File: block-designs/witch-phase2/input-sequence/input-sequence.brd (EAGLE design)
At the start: 160 x 100 mm, 21 parts, among them IC1 74AHC1G08DBV, IC10 741G175, IC11 741G175, IC12 741G175, IC13 74AHC1G32DBV, IC14 74AHC1G32DBV, IC15 74AHC1G32DBV, IC16 74AHC1G32DBV, IC17 74AHC1G32DBV, IC18 74AHC1G32DBV, IC19 4017D, IC2 74AHC1G08DBV, IC3 74AHC1G08DBV, IC4 74AHC1G08DBV, IC5 74AHC1G08DBV, IC6 74AHC1G08DBV, IC7 741G175, IC8 741G175, IC9 741G175

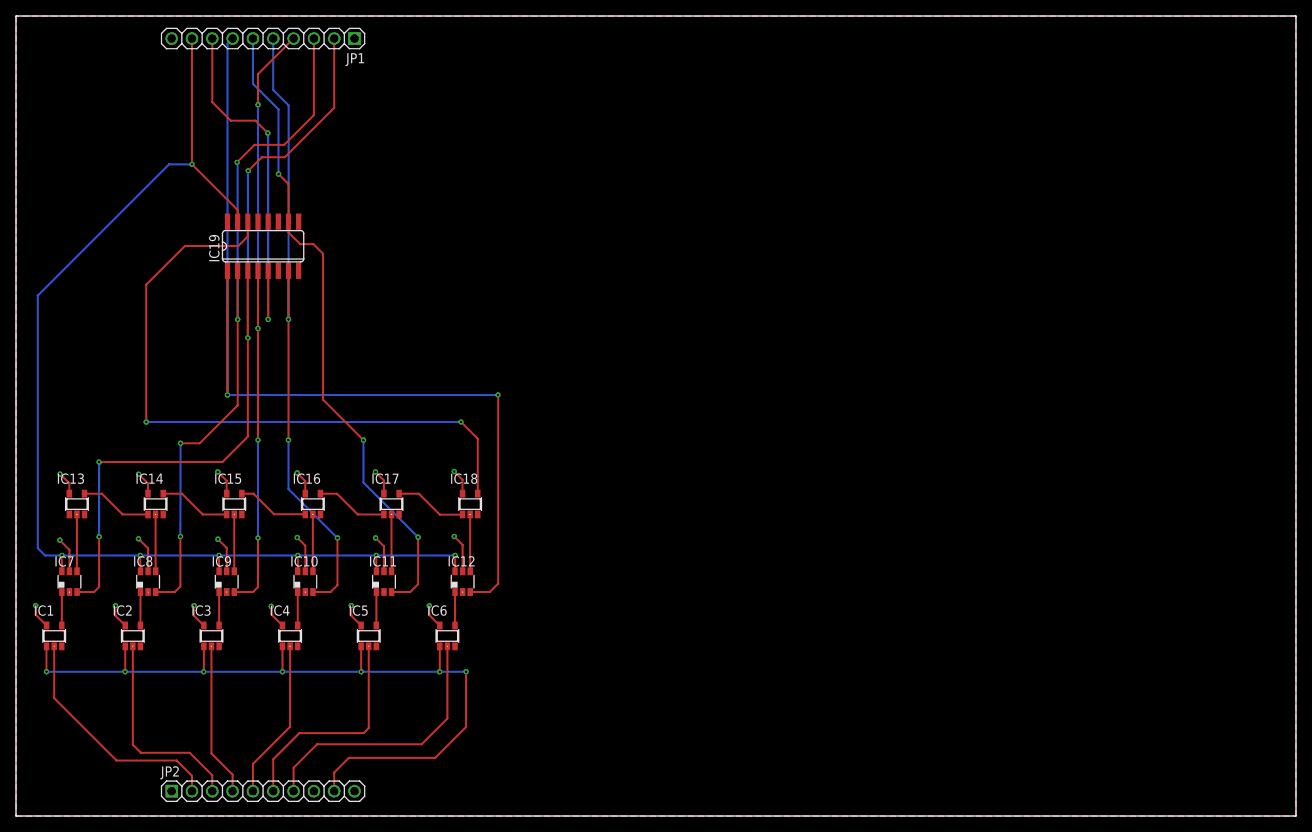
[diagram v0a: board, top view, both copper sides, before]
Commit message: reduce pcb size, add caps, add LEDs
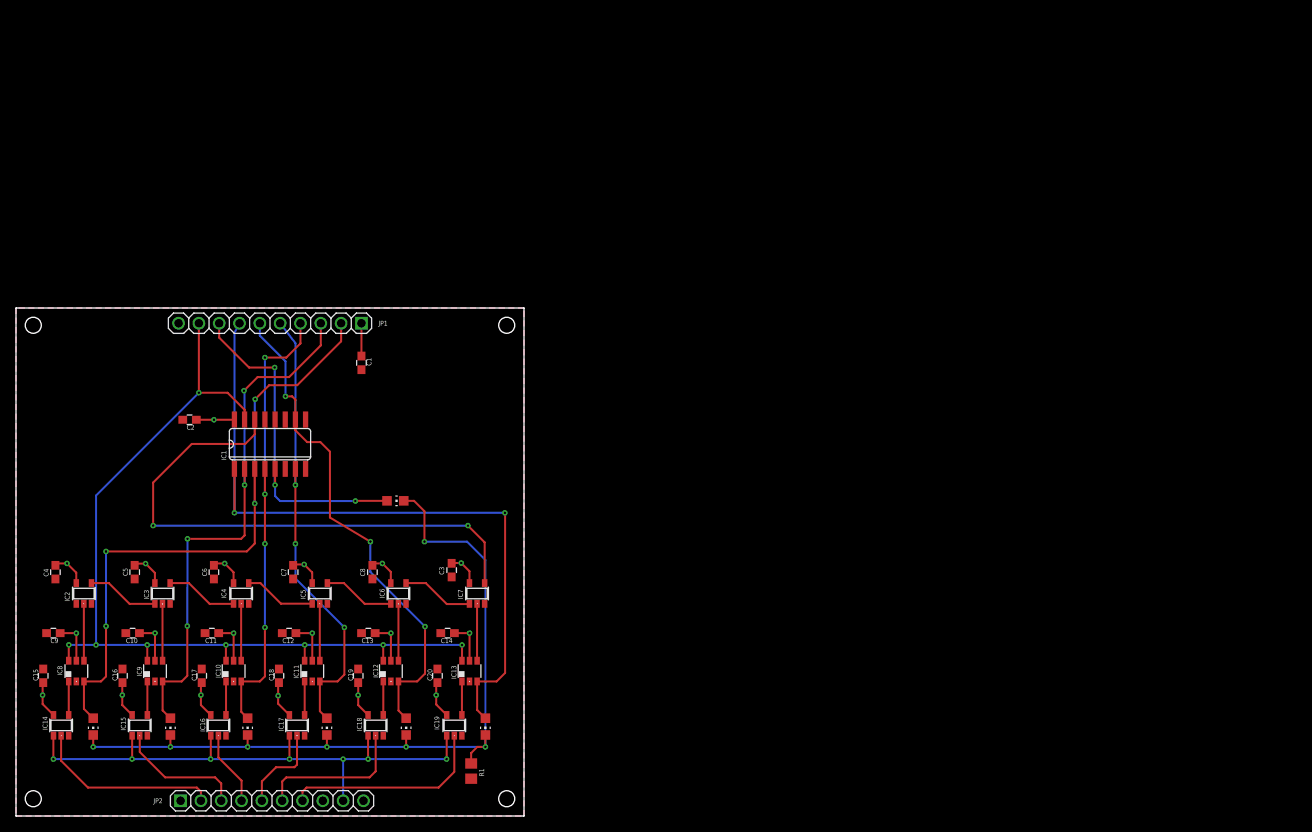
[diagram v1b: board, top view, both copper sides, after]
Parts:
- added C1, C10, C11, C12, C13, C14, C15, C16, C17, C18, C19, C2, C20, C3, C4, C5, C6, C7, C8, C9: 0.1uF, resistor:C0603
- added LED1, LED2, LED3, LED4, LED5, LED6, LED7: RED, led:CHIP-LED0805
- added R1: (no value), resistor:R0805
- IC1: value 74AHC1G08DBV -> 4017D; device 74xx-little-us:SOT23-5 -> 40xx:SO16
- IC13: value 74AHC1G32DBV -> 741G175; device 74xx-little-us:SOT23-5 -> witch-e:DBV_R-PDSO-G6
- IC14, IC15, IC16, IC17, IC18: value 74AHC1G32DBV -> 74AHC1G08DBV
- IC19: value 4017D -> 74AHC1G08DBV; device 40xx:SO16 -> 74xx-little-us:SOT23-5
- IC2, IC3, IC4, IC5, IC6: value 74AHC1G08DBV -> 74AHC1G32DBV
- IC7: value 741G175 -> 74AHC1G32DBV; device witch-e:DBV_R-PDSO-G6 -> 74xx-little-us:SOT23-5
- moved IC19 64.5 mm to (54.8, 11.3)
- moved IC13 53.3 mm to (56.7, 18.1)
- moved IC7 51.0 mm to (57.6, 27.8)
- moved IC1 36.1 mm to (31.8, 46.5)
- moved JP1 35.6 mm to (31.8, 61.6)
- moved IC14 30.1 mm to (5.64, 11.3)
- moved IC15 30.1 mm to (15.5, 11.3)
- moved IC16 30.1 mm to (25.3, 11.3)
- moved IC17 30.1 mm to (35.1, 11.3)
- moved IC18 30.1 mm to (45.0, 11.3)
- moved IC10 14.3 mm to (27.2, 18.1)
- moved IC11 14.3 mm to (37.0, 18.1)
- moved IC12 14.3 mm to (46.9, 18.1)
- moved IC8 14.3 mm to (7.54, 18.1)
- moved IC9 14.3 mm to (17.4, 18.1)
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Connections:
- removed net VDD: IC19.16
- removed net VSS: IC19.8
- new net LED_SINK: LED1.C, LED2.C, LED3.C, LED4.C, LED5.C, LED6.C, LED7.C, R1.2
- net !MCLK: now also IC14.1, IC15.1, IC16.1, IC17.1, IC18.1, IC19.1; no longer IC1.1, IC2.1, IC3.1, IC4.1, IC5.1, IC6.1
- net !RESET: now also IC1.15, IC13.6; no longer IC19.15, IC7.6
- net GND: now also C1.2, C10.2, C11.2, C12.2, C13.2, C14.2, C15.2, C16.2, C17.2, C18.2, C19.2, C2.2, C20.2, C3.2, C4.2, C5.2, C6.2, C7.2, C8.2, C9.2, IC1.13, IC1.8, IC13.2, IC19.3, IC2.1, IC7.3, R1.1; no longer IC1.3, IC13.1, IC13.3, IC19.13, IC7.2
- net N$1: now also IC15.4, IC9.1; no longer IC2.4, IC8.1
- net N$2: now also IC14.4, IC8.1; no longer IC1.4, IC7.1
- net N$3: now also IC10.1, IC16.4; no longer IC3.4, IC9.1
- net N$4: now also IC11.1, IC17.4; no longer IC10.1, IC4.4
- net N$5: now also IC12.1, IC18.4; no longer IC11.1, IC5.4
- net N$6: now also IC13.1, IC19.4; no longer IC12.1, IC6.4
- net NEXT1: now also IC2.4, IC3.1; no longer IC13.4, IC14.1
- net NEXT2: now also IC3.4, IC4.1; no longer IC14.4, IC15.1
- net NEXT3: now also IC4.4, IC5.1; no longer IC15.4, IC16.1
- net NEXT4: now also IC5.4, IC6.1; no longer IC16.4, IC17.1
- net NEXT5: now also IC6.4, IC7.1; no longer IC17.4, IC18.1
- net NEXT6: now also IC1.14, IC7.4; no longer IC18.4, IC19.14
- net SEQ1: now also IC1.3, IC8.3, LED2.A; no longer IC19.3, IC7.3
- net SEQ2: now also IC1.2, IC9.3, LED3.A; no longer IC19.2, IC8.3
- net SEQ3: now also IC1.4, IC10.3, LED4.A; no longer IC19.4, IC9.3
- net SEQ4: now also IC1.7, IC11.3, LED5.A; no longer IC10.3, IC19.7
- net SEQ5: now also IC1.10, IC12.3, LED6.A; no longer IC11.3, IC19.10
- net SEQ6: now also IC1.1, IC13.3, LED7.A; no longer IC12.3, IC19.1
- net SEQ7: now also IC1.5, LED1.A; no longer IC19.5
- net STEP1: now also IC2.2, IC8.4; no longer IC13.2, IC7.4
- net STEP2: now also IC3.2, IC9.4; no longer IC14.2, IC8.4
- net STEP3: now also IC10.4, IC4.2; no longer IC15.2, IC9.4
- net STEP4: now also IC11.4, IC5.2; no longer IC10.4, IC16.2
- net STEP5: now also IC12.4, IC6.2; no longer IC11.4, IC17.2
- net STEP6: now also IC13.4, IC7.2; no longer IC12.4, IC18.2
- net VAL1: now also IC14.2; no longer IC1.2
- net VAL2: now also IC15.2; no longer IC2.2
- net VAL3: now also IC16.2; no longer IC3.2
- net VAL4: now also IC17.2; no longer IC4.2
- net VAL5: now also IC18.2; no longer IC5.2
- net VAL6: now also IC19.2; no longer IC6.2
- net VCC: now also C1.1, C10.1, C11.1, C12.1, C13.1, C14.1, C15.1, C16.1, C17.1, C18.1, C19.1, C2.1, C20.1, C3.1, C4.1, C5.1, C6.1, C7.1, C8.1, C9.1, IC1.16, IC19.5; no longer IC1.5
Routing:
- net LED_SINK: track 0.00 -> 100.2 mm, vias 0 -> 7
- net !RESET: track 147.3 -> 114.4 mm, vias 7 -> 8
- net VCC: track 63.8 -> 94.8 mm, vias 18 -> 19
- net SEQ6: track 121.7 -> 92.2 mm
- net !MCLK: track 99.7 -> 71.9 mm
- net SEQ4: track 81.2 -> 57.5 mm
- net SEQ3: track 80.8 -> 58.9 mm
- net SEQ1: track 102.9 -> 81.1 mm
- net SEQ2: track 88.5 -> 67.7 mm
- net SEQ5: track 81.4 -> 63.3 mm
- net NEXT6: track 83.4 -> 69.8 mm
- net VAL3: track 19.2 -> 9.33 mm
- net VAL2: track 25.8 -> 16.0 mm
- net VAL4: track 20.0 -> 11.3 mm
- net VAL5: track 27.8 -> 19.1 mm
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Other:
- board size 160 x 100 mm -> 63.5 x 63.5 mm
- board text added: "1"
- board text added: "2"
- board text added: "3"
- board text added: "4"
- board text added: "5"
- board text added: "DONE"
- board text added: "EXE"
- board text added: "Input Sequencer"

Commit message: updated layout and added inverter for reset signals
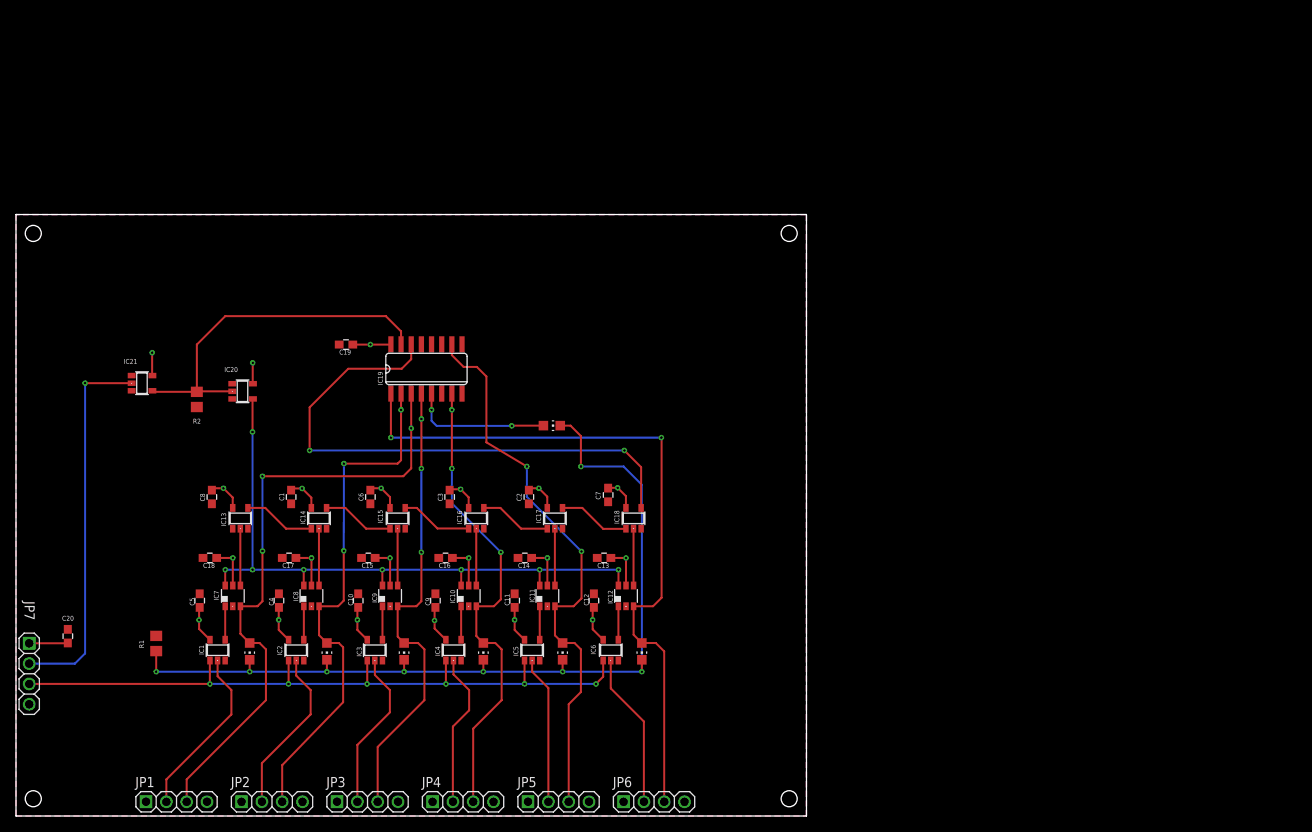
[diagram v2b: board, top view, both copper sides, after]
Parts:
- added IC20, IC21: 74LVC1G14DBV, 74xx-little-us:SOT23-5
- added JP3, JP4, JP5, JP6, JP7: (no value), custom-pinhead:1X04
- added R2: (no value), resistor:R0805
- IC1: value 4017D -> 74AHC1G08DBV; device 40xx:SO16 -> 74xx-little-us:SOT23-5
- IC13: value 741G175 -> 74AHC1G32DBV; device witch-e:DBV_R-PDSO-G6 -> 74xx-little-us:SOT23-5
- IC14, IC15, IC16, IC17, IC18: value 74AHC1G08DBV -> 74AHC1G32DBV
- IC19: value 74AHC1G08DBV -> 4017D; device 74xx-little-us:SOT23-5 -> 40xx:SO16
- IC2, IC3, IC4, IC5, IC6: value 74AHC1G32DBV -> 74AHC1G08DBV
- IC7: value 74AHC1G32DBV -> 741G175; device 74xx-little-us:SOT23-5 -> witch-e:DBV_R-PDSO-G6
- JP1, JP2: device pinhead:1X10 -> custom-pinhead:1X04
- moved JP1 60.9 mm to (20.1, 1.78), turned to 0 degrees
- moved C9 47.9 mm to (52.4, 26.9), turned to 90 degrees
- moved C20 46.5 mm to (6.48, 22.5)
- moved IC19 44.7 mm to (51.3, 55.9)
- moved C2 43.5 mm to (64.1, 39.9), turned to 270 degrees
- moved C15 43.2 mm to (44.0, 32.3), turned to 180 degrees
- moved C16 43.0 mm to (53.7, 32.3), turned to 180 degrees
- moved R1 42.5 mm to (17.5, 21.6), turned to 270 degrees
- moved C19 41.4 mm to (41.2, 58.9), turned to 180 degrees
- moved IC14 41.3 mm to (37.9, 37.2)
- moved IC18 41.3 mm to (77.2, 37.2)
- moved IC15 41.3 mm to (47.7, 37.2)
- moved IC16 41.3 mm to (57.5, 37.2)
- moved IC17 41.3 mm to (67.4, 37.2)
- moved C7 40.5 mm to (74.0, 40.1)
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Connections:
- removed net SEQ1: IC1.3, IC8.3, JP1.2, LED2.A
- removed net SEQ2: IC1.2, IC9.3, JP1.3, LED3.A
- removed net SEQ3: IC1.4, IC10.3, JP1.4, LED4.A
- removed net SEQ4: IC1.7, IC11.3, JP1.5, LED5.A
- removed net SEQ5: IC1.10, IC12.3, JP1.6, LED6.A
- removed net SEQ6: IC1.1, IC13.3, JP1.7, LED7.A
- removed net SEQ7: IC1.5, JP1.8, LED1.A
- new net !CLEAR: IC21.2, JP7.2
- new net RESET: IC19.15, IC20.2, IC21.4, R2.2
- new net SEL1: IC19.3, IC7.3, JP1.3, LED1.A
- new net SEL2: IC19.2, IC8.3, JP2.3, LED2.A
- new net SEL3: IC19.4, IC9.3, JP3.3, LED3.A
- new net SEL4: IC10.3, IC19.7, JP4.3, LED4.A
- new net SEL5: IC11.3, IC19.10, JP5.3, LED5.A
- new net SEL6: IC12.3, IC19.1, JP6.3, LED6.A
- new net SEL7: IC19.5, LED7.A
- net !MCLK: now also IC1.1, IC2.1, IC3.1, IC4.1, IC5.1, IC6.1, JP7.3; no longer IC14.1, IC15.1, IC16.1, IC17.1, IC18.1, IC19.1, JP2.9
- net !RESET: now also IC20.4, IC7.6; no longer IC1.15, IC13.6, JP1.9
- net GND: now also IC1.3, IC13.1, IC13.3, IC19.13, IC19.8, IC20.3, IC21.3, IC7.2, JP1.4, JP2.4, JP3.4, JP4.4, JP5.4, JP6.4, JP7.4, R2.1; no longer IC1.13, IC1.8, IC13.2, IC19.3, IC2.1, IC7.3, JP1.10, JP2.10
- net N$1: now also IC2.4, IC8.1; no longer IC15.4, IC9.1
- net N$2: now also IC1.4, IC7.1; no longer IC14.4, IC8.1
- net N$3: now also IC3.4, IC9.1; no longer IC10.1, IC16.4
- net N$4: now also IC10.1, IC4.4; no longer IC11.1, IC17.4
- net N$5: now also IC11.1, IC5.4; no longer IC12.1, IC18.4
- net N$6: now also IC12.1, IC6.4; no longer IC13.1, IC19.4
- net NEXT1: now also IC13.4, IC14.1; no longer IC2.4, IC3.1
- net NEXT2: now also IC14.4, IC15.1; no longer IC3.4, IC4.1
- net NEXT3: now also IC15.4, IC16.1; no longer IC4.4, IC5.1
- net NEXT4: now also IC16.4, IC17.1; no longer IC5.4, IC6.1
- net NEXT5: now also IC17.4, IC18.1; no longer IC6.4, IC7.1
- net NEXT6: now also IC18.4, IC19.14; no longer IC1.14, IC7.4
- net STEP1: now also IC13.2, IC7.4; no longer IC2.2, IC8.4
- net STEP2: now also IC14.2, IC8.4; no longer IC3.2, IC9.4
- net STEP3: now also IC15.2, IC9.4; no longer IC10.4, IC4.2
- net STEP4: now also IC10.4, IC16.2; no longer IC11.4, IC5.2
- net STEP5: now also IC11.4, IC17.2; no longer IC12.4, IC6.2
- net STEP6: now also IC12.4, IC18.2; no longer IC13.4, IC7.2
- net VAL1: now also IC1.2, JP1.2; no longer IC14.2, JP2.2
- net VAL2: now also IC2.2, JP2.2; no longer IC15.2, JP2.3
- net VAL3: now also IC3.2, JP3.2; no longer IC16.2, JP2.4
- net VAL4: now also IC4.2, JP4.2; no longer IC17.2, JP2.5
- net VAL5: now also IC5.2, JP5.2; no longer IC18.2, JP2.6
- net VAL6: now also IC6.2, JP6.2; no longer IC19.2, JP2.7
- net VCC: now also IC1.5, IC19.16, IC20.5, IC21.5, JP3.1, JP4.1, JP5.1, JP6.1, JP7.1; no longer IC1.16, IC19.5
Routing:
- net SEQ6: track 92.2 -> 0.00 mm, vias 2 -> 0
- net SEL6: track 0.00 -> 90.3 mm, vias 0 -> 2
- net SEQ1: track 81.1 -> 0.00 mm, vias 4 -> 0
- net SEL1: track 0.00 -> 77.6 mm, vias 0 -> 3
- net SEL5: track 0.00 -> 71.2 mm, vias 0 -> 2
- net SEQ2: track 67.7 -> 0.00 mm, vias 4 -> 0
- net SEL2: track 0.00 -> 65.8 mm, vias 0 -> 3
- net SEQ5: track 63.3 -> 0.00 mm, vias 3 -> 0
- net SEL4: track 0.00 -> 59.8 mm, vias 0 -> 3
- net SEQ3: track 58.9 -> 0.00 mm, vias 4 -> 0
- net SEL3: track 0.00 -> 58.4 mm, vias 0 -> 3
- net SEQ4: track 57.5 -> 0.00 mm, vias 3 -> 0
- net !CLEAR: track 0.00 -> 47.1 mm, vias 0 -> 1
- net RESET: track 0.00 -> 45.4 mm
- net SEQ7: track 42.7 -> 0.00 mm, vias 3 -> 0
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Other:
- board size 63.5 x 63.5 mm -> 98.8 x 75.2 mm

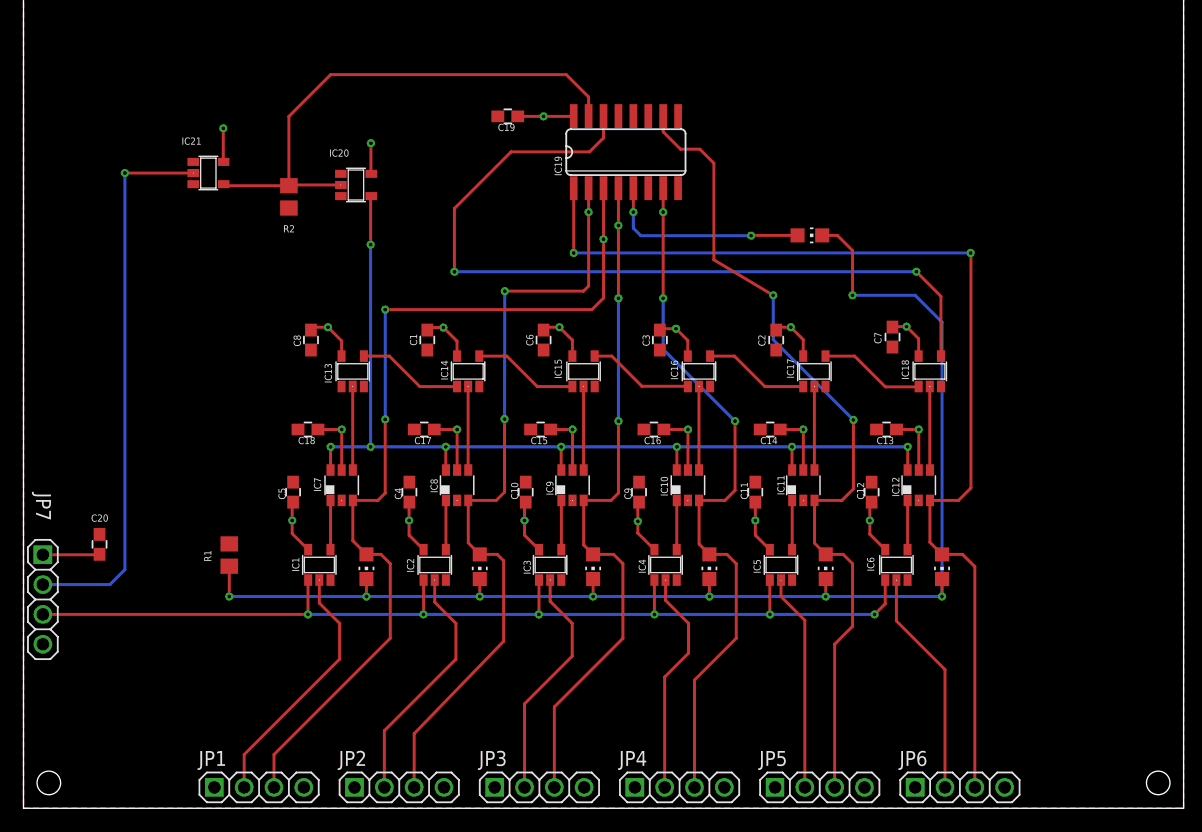
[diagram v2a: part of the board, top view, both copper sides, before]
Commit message: rework of cabling for reset, exec, power, and key-up detection
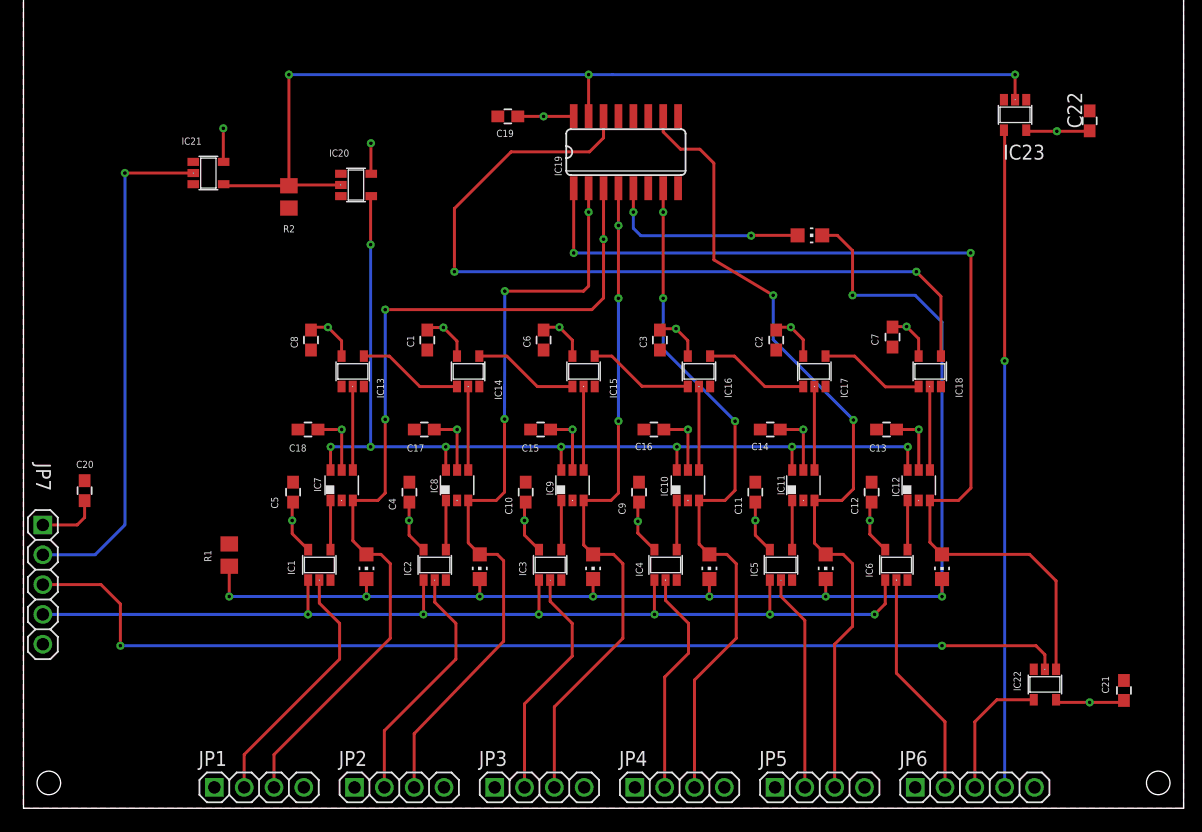
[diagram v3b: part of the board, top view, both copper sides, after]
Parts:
- added C21, C22: 0.1uF, resistor:C0603
- added IC22: 74AHC1G08DBV, 74xx-little-us:SOT23-5
- added IC23: 74LVC1G14DBV, 74xx-little-us:SOT23-5
- JP6, JP7: device custom-pinhead:1X04 -> custom-pinhead:1X05
- moved C20 4.75 mm to (5.21, 27.1)
- moved JP7 1.27 mm to (1.65, 19.1)
- moved JP6 1.27 mm to (81.0, 1.78)
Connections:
- removed net !MCLK: IC1.1, IC2.1, IC3.1, IC4.1, IC5.1, IC6.1, JP7.3
- new net !KEY: IC1.1, IC2.1, IC3.1, IC4.1, IC5.1, IC6.1, JP7.4
- new net !RST_OUT: IC23.4, JP6.4
- new net EXEC: IC22.2, JP7.3
- new net N$7: IC22.4, JP6.3
- net GND: now also C21.2, C22.2, IC22.3, IC23.3, JP6.5, JP7.5; no longer JP6.4, JP7.4
- net RESET: now also IC23.2
- net SEL6: now also IC22.1; no longer JP6.3
- net VCC: now also C21.1, C22.1, IC22.5, IC23.5
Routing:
- net EXEC: track 0.00 -> 91.1 mm, vias 0 -> 2
- net !MCLK: track 88.8 -> 0.00 mm, vias 6 -> 0
- net !KEY: track 0.00 -> 88.8 mm, vias 0 -> 6
- net !RST_OUT: track 0.00 -> 56.0 mm, vias 0 -> 1
- net RESET: track 45.4 -> 87.0 mm, vias 0 -> 3
- net VCC: track 101.1 -> 112.9 mm, vias 21 -> 23
- net N$7: track 0.00 -> 11.4 mm
- net SEL6: track 90.3 -> 86.5 mm
- net !CLEAR: track 47.1 -> 43.8 mm
